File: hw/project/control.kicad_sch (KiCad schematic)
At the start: 48 parts, among them SW1 RESET, SW2 BOOT0, U7 STSPIN32G4, X1 32MHZ 10PF

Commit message: Continue phase voltage circuit tom
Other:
- note added: "TODO: CHANGE BASED ON FINAL VBUS MAX"
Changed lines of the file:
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@@
+		)
+	)
+	(text "TODO: CHANGE BASED ON FINAL VBUS MAX"
+		(exclude_from_sim no)
+		(at 160.02 140.462 0)
+		(effects
+			(font
+				(size 1.27 1.27)
+				(color 255 4 4 1)
+			)
 		)
 	)
@@
 		)
 	)
-	(text_box "Bus Voltage Monitoring\n\nVM_max = 78V, but take as 82.5V to avoid clipping\n\n82.5V / 3.3V = 25.0 = Rbus_2 / (Rbus_1 + Rbus_2) => Rbus_1 / Rbus_2 = 24.0"
+	(text_box "Bus Voltage Monitoring\n\n- VM_max = 78V, but take as 82.5V to avoid clipping\n- 82.5V / 3.3V = 25.0 = Rbus_2 / (Rbus_1 + Rbus_2) => Rbus_1 / Rbus_2 = 24.0\n- Used to determine Virtual Neutral Point in-software as opposed to hardware"
 		(exclude_from_sim no)
 		(at 167.64 135.89 0)
@@
 		)
 		(pin "18"
+			(alternate "SPI1_SCK")
 		)
 		(pin "6"
@@
 		)
 		(pin "16"
+			(alternate "OPAMP1_VINM")
 		)
 		(pin "24"

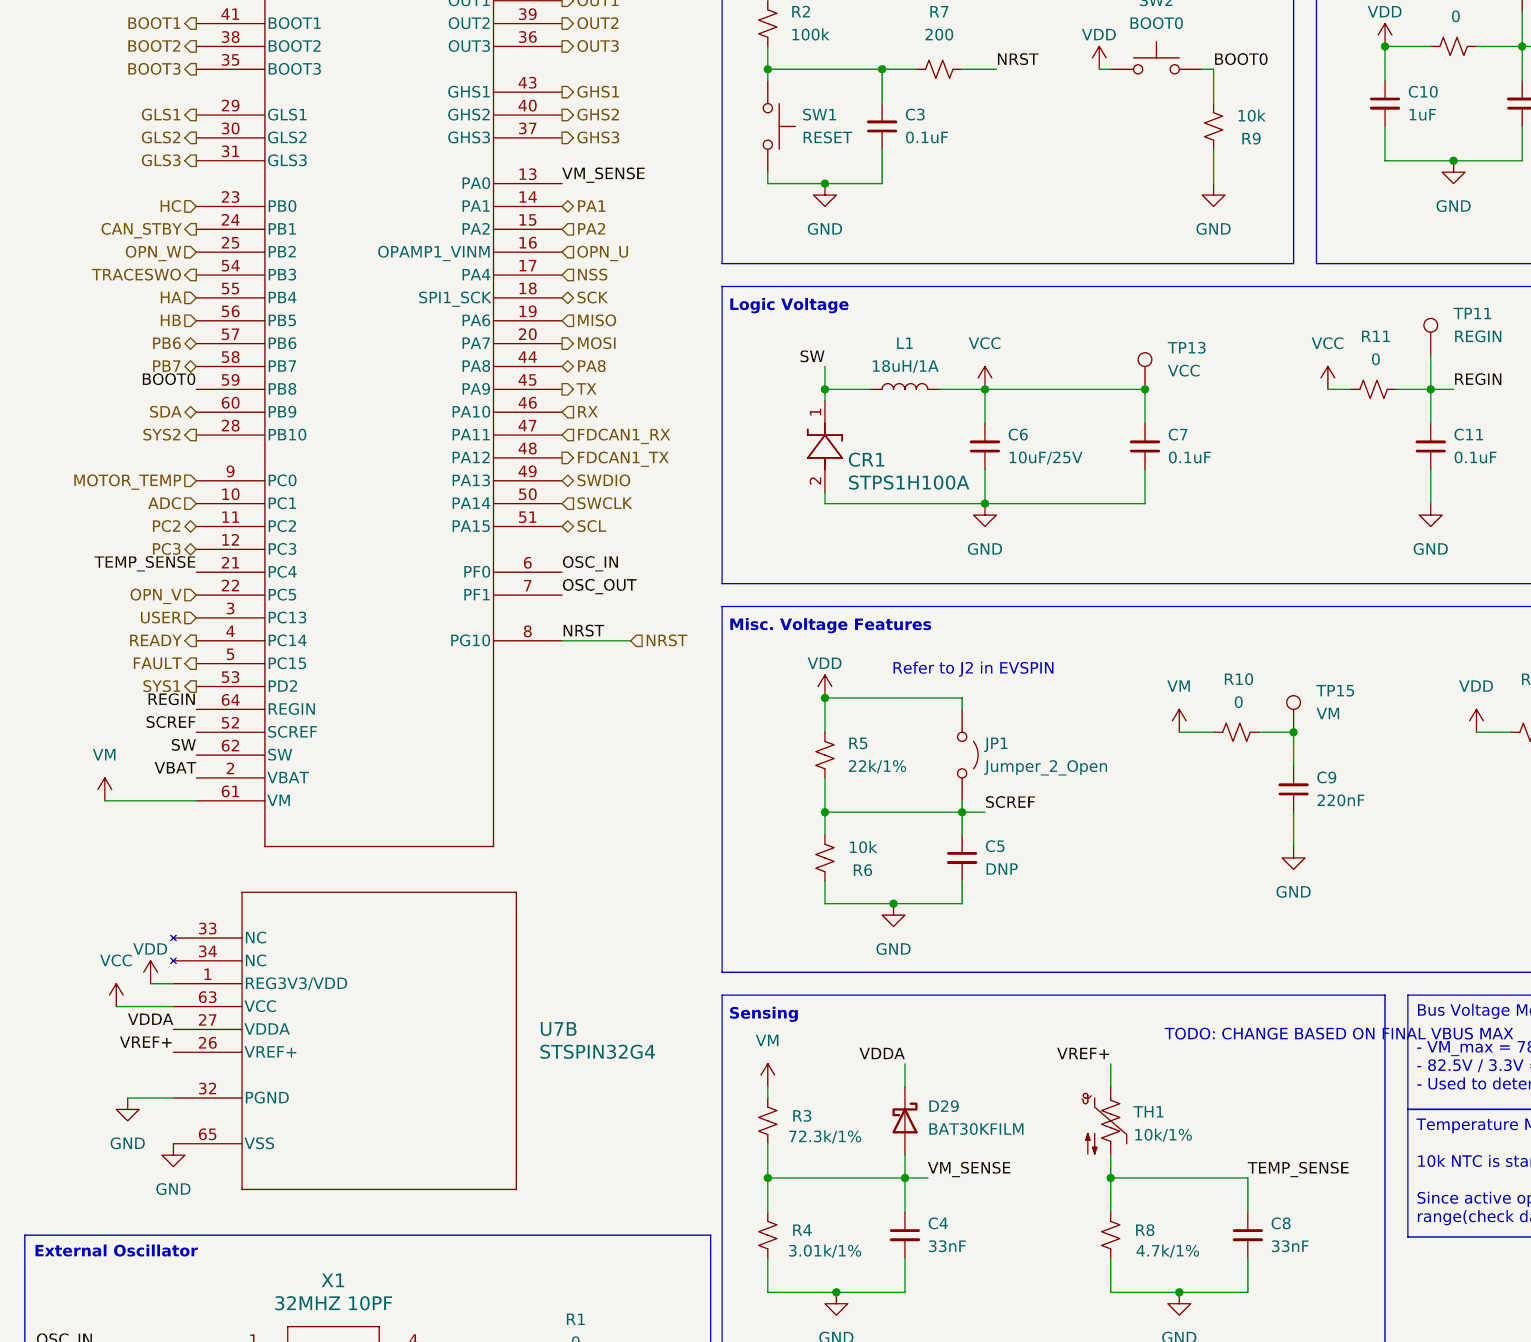
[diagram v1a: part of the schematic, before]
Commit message: Add phase voltage first draft
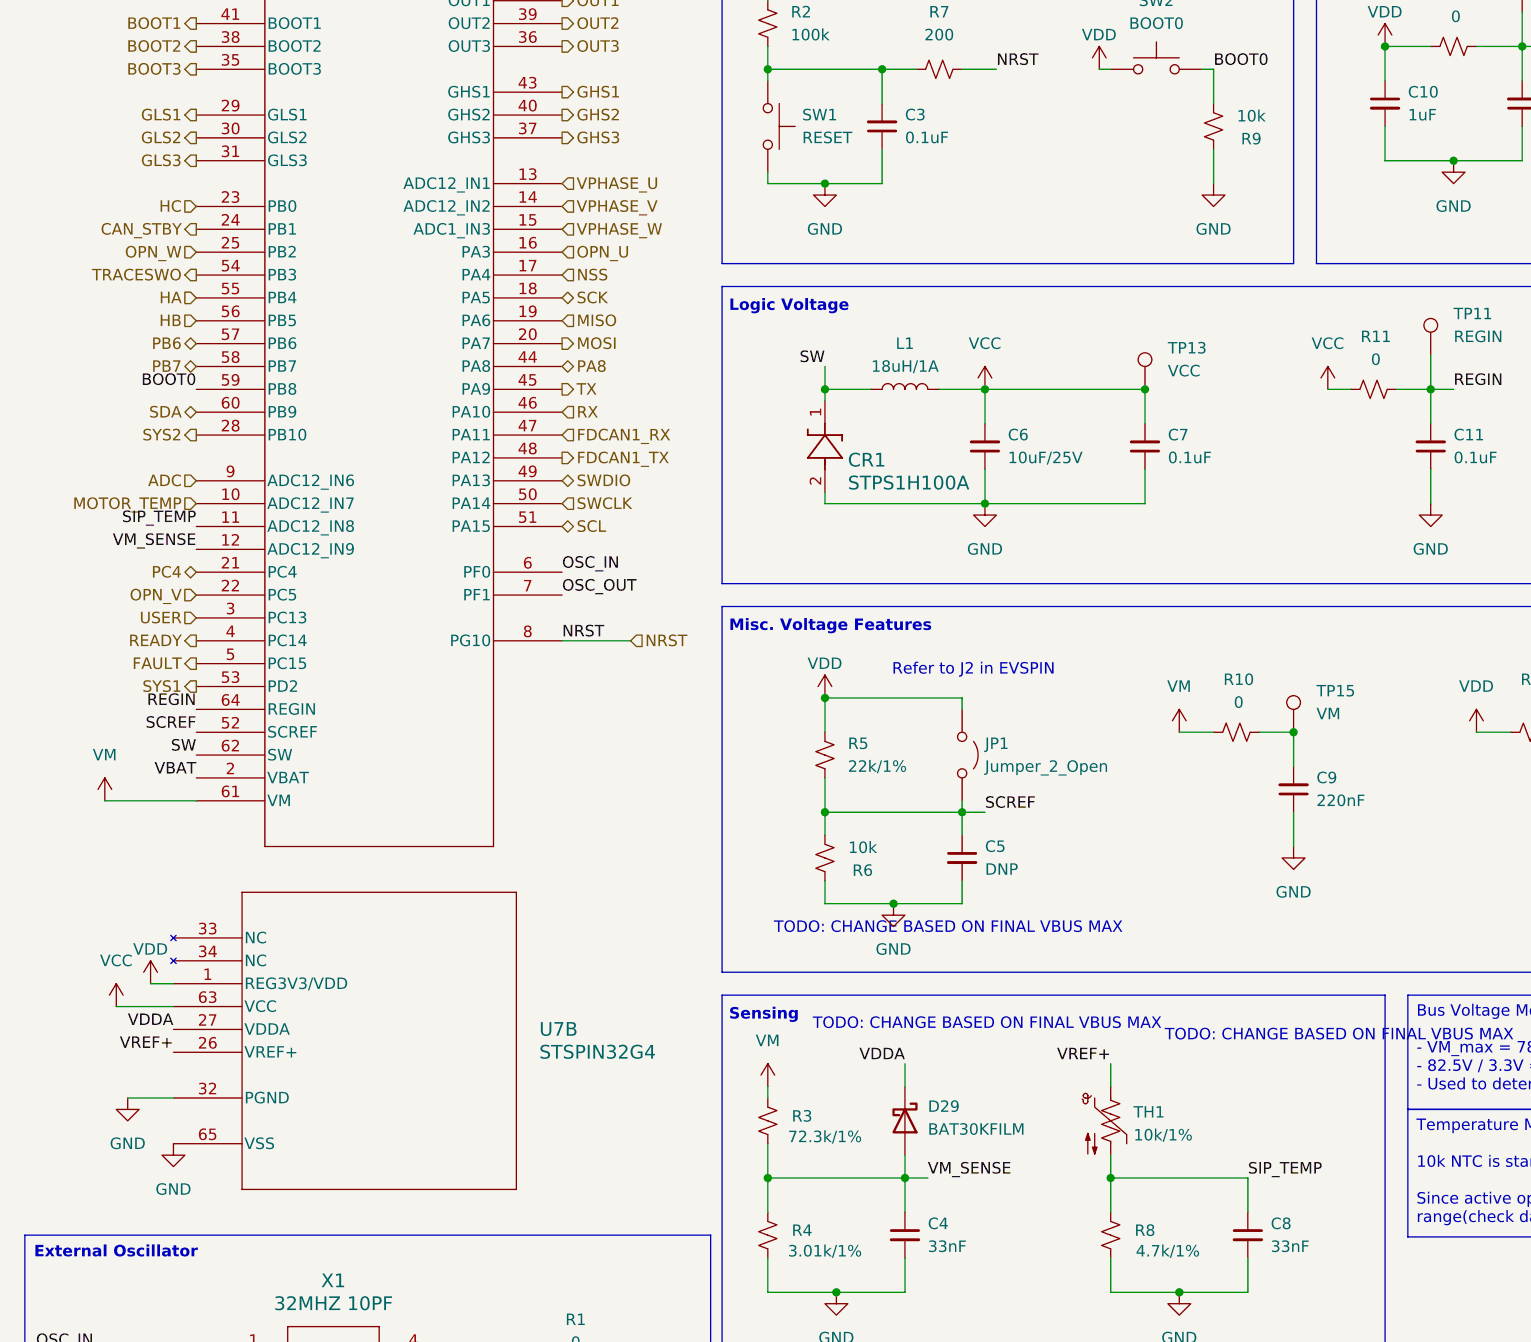
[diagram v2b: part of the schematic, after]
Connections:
- net PC3 is gone; now on net VM_SENSE: U7.12 (PC3)
- net ADC: now also U7.9 (PC0); no longer U7.10 (PC1)
- net MOTOR_TEMP: now also U7.10 (PC1); no longer U7.9 (PC0)
- net VM_SENSE: no longer U7.13 (PA0)
- net PA1 renamed VPHASE_V
- net PA2 renamed VPHASE_W
- net PC2 renamed SIP_TEMP
- net SIP_TEMP: now also C8.1, R8.1, TH1.2
- removed net TEMP_SENSE: C8.1, R8.1, TH1.2, U7.21 (PC4)
- new net PC4: U7.21 (PC4)
- new net VPHASE_U: U7.13 (PA0)
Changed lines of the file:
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@@
+		)
+	)
+	(text "TODO: CHANGE BASED ON FINAL VBUS MAX"
+		(exclude_from_sim no)
+		(at 120.904 139.192 0)
+		(effects
+			(font
+				(size 1.27 1.27)
+				(color 255 4 4 1)
+			)
 		)
 	)
@@
 			)
 			(justify left top)
+		)
+	)
+	(text "TODO: CHANGE BASED ON FINAL VBUS MAX"
+		(exclude_from_sim no)
+		(at 116.586 128.524 0)
+		(effects
+			(font
+				(size 1.27 1.27)
+				(color 255 4 4 1)
+			)
 		)
 	)
@@
 		)
 	)
-	(label "TEMP_SENSE"
-		(at 33.02 88.9 180)
+	(label "SIP_TEMP"
+		(at 33.02 83.82 180)
 		(effects
 			(font
@@
 	)
 	(label "VM_SENSE"
-		(at 73.66 45.72 0)
-		(effects
-			(font
-				(size 1.27 1.27)
-			)
-			(justify left bottom)
+		(at 33.02 86.36 180)
+		(effects
+			(font
+				(size 1.27 1.27)
+			)
+			(justify right bottom)
 		)
 	)
@@
 		)
 	)
-	(label "TEMP_SENSE"
+	(label "SIP_TEMP"
 		(at 149.86 156.21 0)
 		(effects
@@
 		)
 	)
-	(hierarchical_label "PA2"
-		(shape input)
-		(at 73.66 50.8 0)
-		(effects
-			(font
-				(size 1.27 1.27)
-			)
-			(justify left)
-		)
-	)
 	(hierarchical_label "CAN_STBY"
 		(shape output)
@@
 	(hierarchical_label "ADC"
 		(shape input)
-		(at 33.02 81.28 180)
+		(at 33.02 78.74 180)
 		(effects
 			(font
@@
 		)
 	)
-	(hierarchical_label "PC2"
+	(hierarchical_label "PC4"
 		(shape bidirectional)
-		(at 33.02 83.82 180)
+		(at 33.02 88.9 180)
 		(effects
 			(font
@@
 		)
 	)
+	(hierarchical_label "VPHASE_W"
+		(shape input)
+		(at 73.66 50.8 0)
+		(effects
+			(font
+				(size 1.27 1.27)
+			)
+			(justify left)
+		)
+	)
 	(hierarchical_label "SWDIO"
 		(shape bidirectional)
@@
 	(hierarchical_label "MOTOR_TEMP"
 		(shape input)
-		(at 33.02 78.74 180)
+		(at 33.02 81.28 180)
 		(effects
 			(font
@@
 		)
 	)
-	(hierarchical_label "PA1"
-		(shape bidirectional)
+	(hierarchical_label "VPHASE_V"
+		(shape input)
 		(at 73.66 48.26 0)
 		(effects
@@
 		)
 	)
-	(hierarchical_label "PC3"
-		(shape bidirectional)
-		(at 33.02 86.36 180)
-		(effects
-			(font
-				(size 1.27 1.27)
-			)
-			(justify right)
-		)
-	)
 	(hierarchical_label "OUT1"
 		(shape output)
@@
 			)
 			(justify right)
+		)
+	)
+	(hierarchical_label "VPHASE_U"
+		(shape input)
+		(at 73.66 45.72 0)
+		(effects
+			(font
+				(size 1.27 1.27)
+			)
+			(justify left)
 		)
 	)
@@
 		)
 		(pin "11"
+			(alternate "ADC12_IN8")
 		)
 		(pin "39"
 		)
 		(pin "9"
+			(alternate "ADC12_IN6")
 		)
 		(pin "8"
@@
 		)
 		(pin "18"
-			(alternate "SPI1_SCK")
 		)
 		(pin "6"
 		)
 		(pin "13"
+			(alternate "ADC12_IN1")
 		)
 		(pin "15"
+			(alternate "ADC1_IN3")
 		)
 		(pin "19"
@@
 		)
 		(pin "14"
+			(alternate "ADC12_IN2")
 		)
 		(pin "12"
+			(alternate "ADC12_IN9")
 		)
 		(pin "10"
+			(alternate "ADC12_IN7")
 		)
 		(pin "16"
-			(alternate "OPAMP1_VINM")
 		)
 		(pin "24"

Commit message: Remap hall sensor pins
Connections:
- net PA8 is gone; now on net CAN_STBY: U7.44 (PA8)
- net PC4 is gone; now on net ADC: U7.21 (PC4)
- net ADC: no longer U7.9 (PC0)
- net CAN_STBY: no longer U7.24 (PB1)
- net HA: now also U7.13 (PA0); no longer U7.55 (PB4)
- net HB: now also U7.14 (PA1); no longer U7.56 (PB5)
- net HC: now also U7.15 (PA2); no longer U7.23 (PB0)
- net MOTOR_TEMP: now also U7.24 (PB1); no longer U7.10 (PC1)
- net SIP_TEMP: now also U7.23 (PB0); no longer U7.11 (PC2)
- net VM_SENSE: now also U7.9 (PC0); no longer U7.12 (PC3)
- net VPHASE_U: now also U7.10 (PC1); no longer U7.13 (PA0)
- net VPHASE_V: now also U7.11 (PC2); no longer U7.14 (PA1)
- net VPHASE_W: now also U7.12 (PC3); no longer U7.15 (PA2)
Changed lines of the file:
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@@
 	)
 	(label "SIP_TEMP"
-		(at 33.02 83.82 180)
+		(at 33.02 48.26 180)
 		(effects
 			(font
@@
 	)
 	(label "VM_SENSE"
-		(at 33.02 86.36 180)
+		(at 33.02 78.74 180)
 		(effects
 			(font
@@
 	(hierarchical_label "CAN_STBY"
 		(shape output)
-		(at 33.02 50.8 180)
-		(effects
-			(font
-				(size 1.27 1.27)
-			)
-			(justify right)
+		(at 73.66 66.04 0)
+		(effects
+			(font
+				(size 1.27 1.27)
+			)
+			(justify left)
 		)
 	)
@@
 	(hierarchical_label "HB"
 		(shape input)
-		(at 33.02 60.96 180)
-		(effects
-			(font
-				(size 1.27 1.27)
-			)
-			(justify right)
+		(at 73.66 48.26 0)
+		(effects
+			(font
+				(size 1.27 1.27)
+			)
+			(justify left)
 		)
 	)
@@
 	(hierarchical_label "HC"
 		(shape input)
-		(at 33.02 48.26 180)
-		(effects
-			(font
-				(size 1.27 1.27)
-			)
-			(justify right)
+		(at 73.66 50.8 0)
+		(effects
+			(font
+				(size 1.27 1.27)
+			)
+			(justify left)
 		)
 	)
@@
 	(hierarchical_label "ADC"
 		(shape input)
-		(at 33.02 78.74 180)
+		(at 33.02 88.9 180)
 		(effects
 			(font
@@
 	(hierarchical_label "HA"
 		(shape input)
-		(at 33.02 58.42 180)
-		(effects
-			(font
-				(size 1.27 1.27)
-			)
-			(justify right)
+		(at 73.66 45.72 0)
+		(effects
+			(font
+				(size 1.27 1.27)
+			)
+			(justify left)
 		)
 	)
@@
 			)
 			(justify left)
-		)
-	)
-	(hierarchical_label "PC4"
-		(shape bidirectional)
-		(at 33.02 88.9 180)
-		(effects
-			(font
-				(size 1.27 1.27)
-			)
-			(justify right)
 		)
 	)
@@
 	(hierarchical_label "VPHASE_W"
 		(shape input)
-		(at 73.66 50.8 0)
-		(effects
-			(font
-				(size 1.27 1.27)
-			)
-			(justify left)
+		(at 33.02 86.36 180)
+		(effects
+			(font
+				(size 1.27 1.27)
+			)
+			(justify right)
 		)
 	)
@@
 	(hierarchical_label "MOTOR_TEMP"
 		(shape input)
+		(at 33.02 50.8 180)
+		(effects
+			(font
+				(size 1.27 1.27)
+			)
+			(justify right)
+		)
+	)
+	(hierarchical_label "FDCAN1_TX"
+		(shape output)
+		(at 73.66 76.2 0)
+		(effects
+			(font
+				(size 1.27 1.27)
+			)
+			(justify left)
+		)
+	)
+	(hierarchical_label "GLS2"
+		(shape output)
+		(at 33.02 40.64 180)
+		(effects
+			(font
+				(size 1.27 1.27)
+			)
+			(justify right)
+		)
+	)
+	(hierarchical_label "NRST"
+		(shape input)
+		(at 81.28 96.52 0)
+		(effects
+			(font
+				(size 1.27 1.27)
+			)
+			(justify left)
+		)
+	)
+	(hierarchical_label "FDCAN1_RX"
+		(shape input)
+		(at 73.66 73.66 0)
+		(effects
+			(font
+				(size 1.27 1.27)
+			)
+			(justify left)
+		)
+	)
+	(hierarchical_label "VPHASE_V"
+		(shape input)
+		(at 33.02 83.82 180)
+		(effects
+			(font
+				(size 1.27 1.27)
+			)
+			(justify right)
+		)
+	)
+	(hierarchical_label "GHS2"
+		(shape output)
+		(at 73.66 38.1 0)
+		(effects
+			(font
+				(size 1.27 1.27)
+			)
+			(justify left)
+		)
+	)
+	(hierarchical_label "BOOT3"
+		(shape output)
+		(at 33.02 33.02 180)
+		(effects
+			(font
+				(size 1.27 1.27)
+			)
+			(justify right)
+		)
+	)
+	(hierarchical_label "OPN_U"
+		(shape input)
+		(at 73.66 53.34 0)
+		(effects
+			(font
+				(size 1.27 1.27)
+			)
+			(justify left)
+		)
+	)
+	(hierarchical_label "OUT1"
+		(shape output)
+		(at 73.66 25.4 0)
+		(effects
+			(font
+				(size 1.27 1.27)
+			)
+			(justify left)
+		)
+	)
+	(hierarchical_label "MISO"
+		(shape input)
+		(at 73.66 60.96 0)
+		(effects
+			(font
+				(size 1.27 1.27)
+			)
+			(justify left)
+		)
+	)
+	(hierarchical_label "OUT2"
+		(shape output)
+		(at 73.66 27.94 0)
+		(effects
+			(font
+				(size 1.27 1.27)
+			)
+			(justify left)
+		)
+	)
+	(hierarchical_label "USER"
+		(shape input)
+		(at 33.02 93.98 180)
+		(effects
+			(font
+				(size 1.27 1.27)
+			)
+			(justify right)
+		)
+	)
+	(hierarchical_label "VPHASE_U"
+		(shape input)
 		(at 33.02 81.28 180)
 		(effects
@@
 		)
 	)
-	(hierarchical_label "FDCAN1_TX"
-		(shape output)
-		(at 73.66 76.2 0)
-		(effects
-			(font
-				(size 1.27 1.27)
-			)
-			(justify left)
-		)
-	)
-	(hierarchical_label "GLS2"
-		(shape output)
-		(at 33.02 40.64 180)
-		(effects
-			(font
-				(size 1.27 1.27)
-			)
-			(justify right)
-		)
-	)
-	(hierarchical_label "NRST"
-		(shape input)
-		(at 81.28 96.52 0)
-		(effects
-			(font
-				(size 1.27 1.27)
-			)
-			(justify left)
-		)
-	)
-	(hierarchical_label "FDCAN1_RX"
-		(shape input)
-		(at 73.66 73.66 0)
-		(effects
-			(font
-				(size 1.27 1.27)
-			)
-			(justify left)
-		)
-	)
-	(hierarchical_label "VPHASE_V"
-		(shape input)
-		(at 73.66 48.26 0)
-		(effects
-			(font
-				(size 1.27 1.27)
-			)
-			(justify left)
-		)
-	)
-	(hierarchical_label "GHS2"
-		(shape output)
-		(at 73.66 38.1 0)
-		(effects
-			(font
-				(size 1.27 1.27)
-			)
-			(justify left)
-		)
-	)
-	(hierarchical_label "BOOT3"
-		(shape output)
-		(at 33.02 33.02 180)
-		(effects
-			(font
-				(size 1.27 1.27)
-			)
-			(justify right)
-		)
-	)
-	(hierarchical_label "OPN_U"
-		(shape input)
-		(at 73.66 53.34 0)
-		(effects
-			(font
-				(size 1.27 1.27)
-			)
-			(justify left)
-		)
-	)
-	(hierarchical_label "OUT1"
-		(shape output)
-		(at 73.66 25.4 0)
-		(effects
-			(font
-				(size 1.27 1.27)
-			)
-			(justify left)
-		)
-	)
-	(hierarchical_label "MISO"
-		(shape input)
-		(at 73.66 60.96 0)
-		(effects
-			(font
-				(size 1.27 1.27)
-			)
-			(justify left)
-		)
-	)
-	(hierarchical_label "OUT2"
-		(shape output)
-		(at 73.66 27.94 0)
-		(effects
-			(font
-				(size 1.27 1.27)
-			)
-			(justify left)
-		)
-	)
-	(hierarchical_label "USER"
-		(shape input)
-		(at 33.02 93.98 180)
-		(effects
-			(font
-				(size 1.27 1.27)
-			)
-			(justify right)
-		)
-	)
-	(hierarchical_label "VPHASE_U"
-		(shape input)
-		(at 73.66 45.72 0)
-		(effects
-			(font
-				(size 1.27 1.27)
-			)
-			(justify left)
-		)
-	)
 	(hierarchical_label "OUT3"
 		(shape output)
@@
 		(shape output)
 		(at 73.66 35.56 0)
-		(effects
-			(font
-				(size 1.27 1.27)
-			)
-			(justify left)
-		)
-	)
-	(hierarchical_label "PA8"
-		(shape bidirectional)
-		(at 73.66 66.04 0)
 		(effects
 			(font
@@
 		)
 		(pin "13"
-			(alternate "ADC12_IN1")
+			(alternate "TIM2_CH1")
 		)
 		(pin "15"
-			(alternate "ADC1_IN3")
+			(alternate "TIM2_CH3")
 		)
 		(pin "19"
 		)
 		(pin "23"
+			(alternate "ADC1_IN15")
 		)
 		(pin "21"
+			(alternate "ADC2_IN5")
 		)
 		(pin "7"
 		)
 		(pin "14"
-			(alternate "ADC12_IN2")
+			(alternate "TIM2_CH2")
 		)
 		(pin "12"
@@
 		)
 		(pin "24"
+			(alternate "ADC1_IN12")
 		)
 		(pin "17"

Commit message: Reorg rest of pins
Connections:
- net PB7 is gone; now on net SDA: U7.58 (PB7)
- net SDA: no longer U7.60 (PB9)
- net STATUS1: now reaches U7.55 (PB4)
- net STATUS2: now reaches U7.56 (PB5)
- net SYS1 renamed PD2
- net SYS2 renamed PB10
- new net PB9: U7.60 (PB9)

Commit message: Finalize reset/power buttons and VDDA/VREF+
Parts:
- removed R12: 0, Resistor_SMD:R_0603_1608Metric, symbol Device:R_Small_US
- removed R2: 100k, Resistor_SMD:R_0603_1608Metric, symbol Device:R_Small_US
- removed R7: 200, Resistor_SMD:R_0603_1608Metric, symbol Device:R_Small_US
- added R80: 10k, Resistor_SMD:R_0603_1608Metric, symbol Device:R_Small_US
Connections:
- net BOOT0: now also SW2.1; no longer SW2.2
- net NRST: now also C3.2, SW1.1, R80.2
- net VDD: now also SW2.2, R80.1; no longer SW2.1
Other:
- moved on the sheet: C10, C12, C3, FB1, R9, SW1, SW2, TP1, TP6
